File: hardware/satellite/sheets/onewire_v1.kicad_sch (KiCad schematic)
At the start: 6 parts, among them J6 Conn_01x03, U3 DS2482S-100+

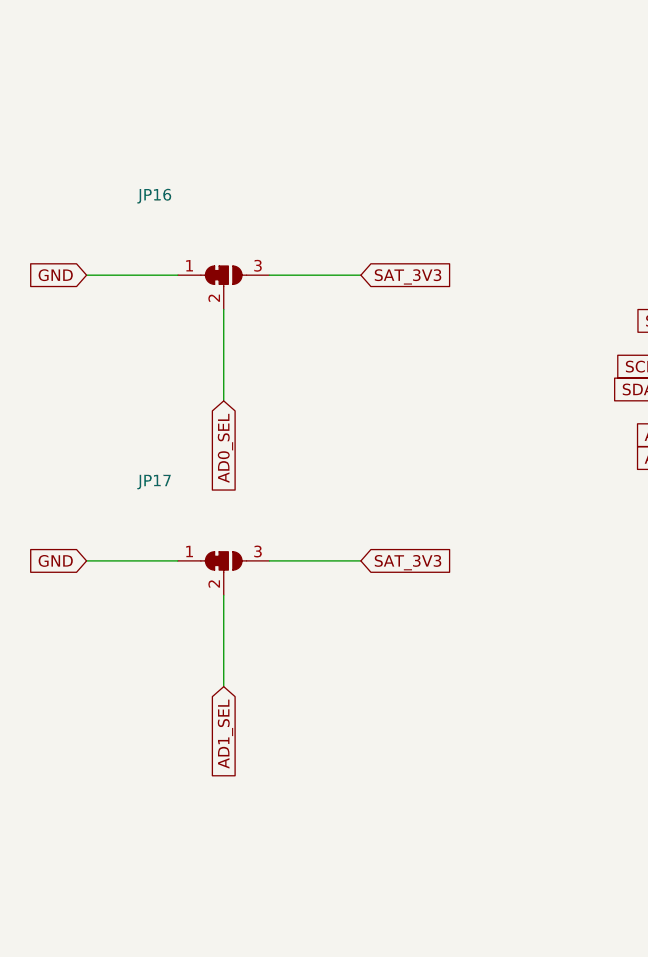
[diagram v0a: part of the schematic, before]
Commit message: Update the jumpers so it is a single symbol and footprint. Add jumper labels. Add CI/CD pipeline for satellite
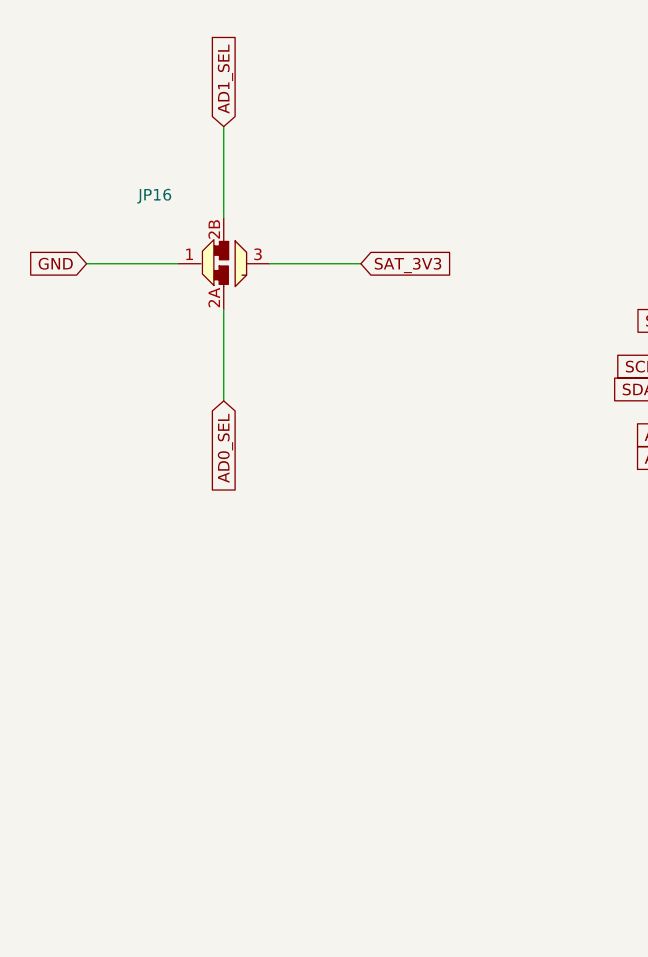
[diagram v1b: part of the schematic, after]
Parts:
- removed JP17: SolderJumper_3_Bridged12, Jumper:SolderJumper-3_P1.3mm_Bridged12_RoundedPad1.0x1.5mm, symbol Jumper:SolderJumper_3_Bridged12
- JP16: value SolderJumper_3_Bridged12 -> Dual Solder Jumper with Both connected to Pin 1.; footprint Jumper:SolderJumper-3_P1.3mm_Bridged12_RoundedPad1.0x1.5mm -> project:SolderJumper-3_P1.3mm_DualAddrSelect_RoundedPad1.0x1.5mm; symbol Jumper:SolderJumper_3_Bridged12 -> project:Dual_SolderJumper_3_Bridged12A_Bridged12B; now left out of the parts list
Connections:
- net AD0_SEL: now also JP16.2A (C); no longer JP16.2 (C)
- net AD1_SEL: now also JP16.2B (C)
